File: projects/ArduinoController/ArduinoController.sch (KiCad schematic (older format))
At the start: 0 parts

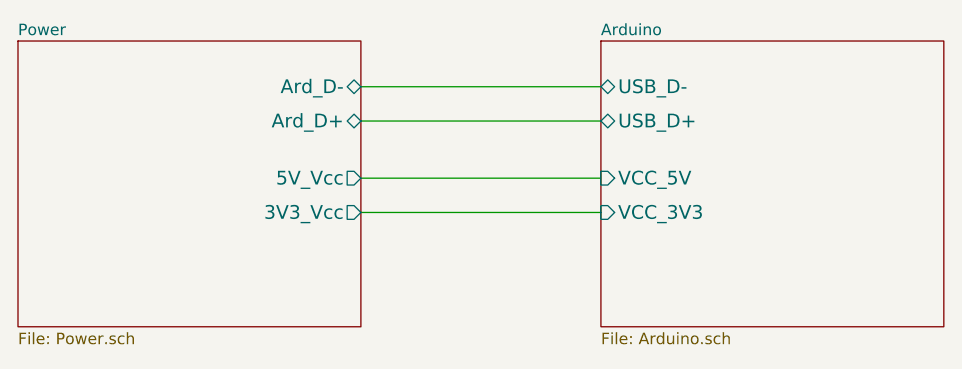
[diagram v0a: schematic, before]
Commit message: working on schematics of Arduino Controller
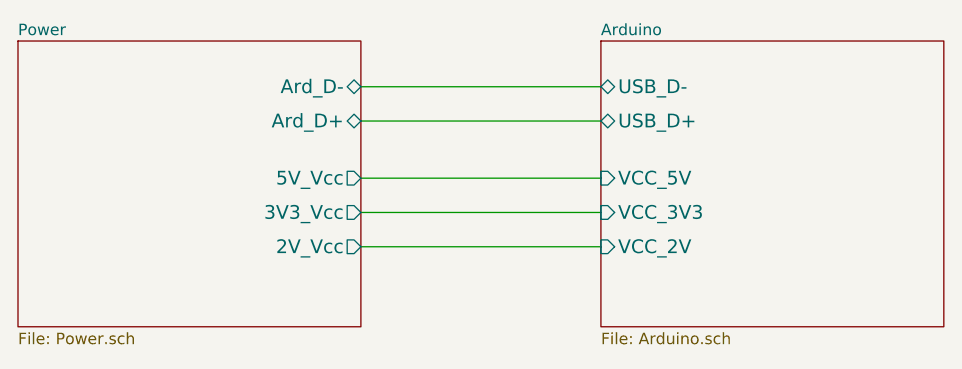
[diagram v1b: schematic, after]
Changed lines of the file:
@@
 F4 "VCC_5V" I L 6325 3450 60
 F5 "VCC_3V3" I L 6325 3600 60
+F6 "VCC_2V" I L 6325 3750 60
 $EndSheet
 $Sheet
@@
 F4 "5V_Vcc" O R 5275 3450 60
 F5 "3V3_Vcc" O R 5275 3600 60
+F6 "2V_Vcc" O R 5275 3750 60
 $EndSheet
 Wire Wire Line
@@
 Wire Wire Line
 	5275 3600 6325 3600
+Wire Wire Line
+	5275 3750 6325 3750
 $EndSCHEMATC
